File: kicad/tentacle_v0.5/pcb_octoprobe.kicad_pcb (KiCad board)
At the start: 2 copper layers, 100 x 165 mm, 736 parts, among them J101 USB-226-BRW, J1302 Conn_02x20, J1303 Conn_02x20, J1501 Conn_02x20, J1502 Conn_01x12, J201 Conn_02x05, J301 USB_C_Receptacle_USB2.0, J501 Conn_02x20, U1001 GAQY221S, U1101 GAQY221S, U1201 GAQY221S, U1401 MT9700, U1501 RP2040, U1502 W25Q32JVS, U1503 TXB0108PW, U201 RP2040, U202 AMS1117-3.3, U203 W25Q32JVS, U301 AMS1117-3.3, U302 USB2514B_Bi, U401 MT9700, U601 GAQY221S, U701 GAQY221S, U801 GAQY221S, U901 GAQY221S, X201 Oscillator-12MHz, Y301 24MHz

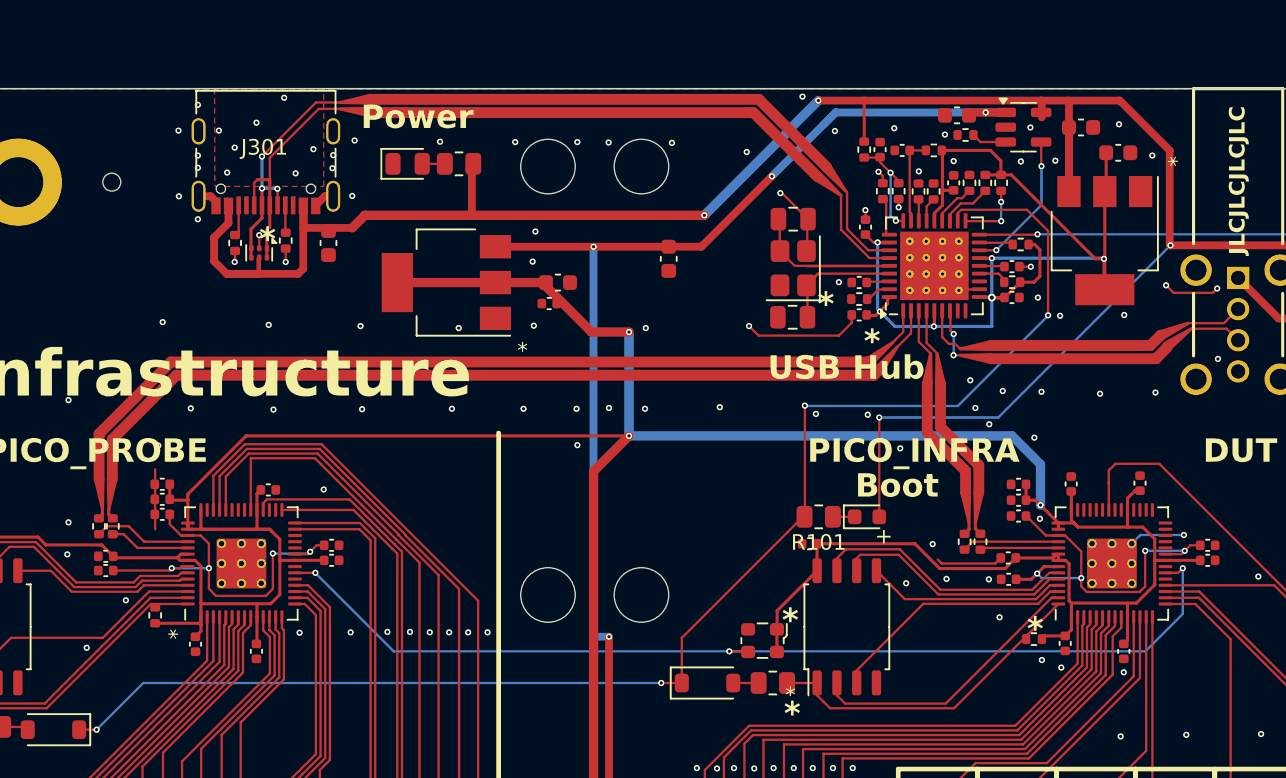
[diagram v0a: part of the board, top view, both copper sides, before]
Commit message: Footprint 'USB Differential': Increase distance
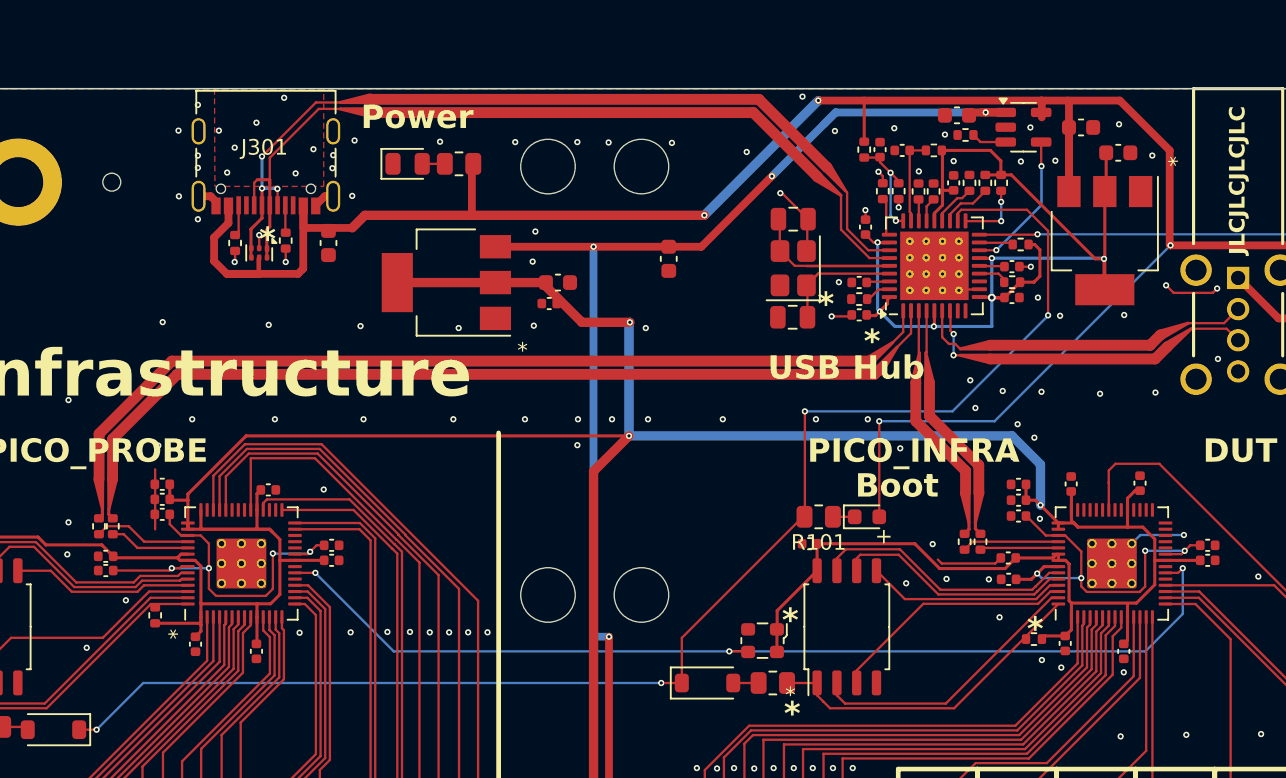
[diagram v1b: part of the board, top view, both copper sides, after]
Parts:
- NT101, NT102, NT103, NT104, NT105, NT106, NT301, NT302: value octoprobe_NetTie_USB_Differential -> NetTie-4_USB_Differential
- moved NT103 0.72 mm to (122.8, 35.2)
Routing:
- net GND: track 192.2 -> 185.9 mm

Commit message: Breadboard: Remove pads from schematic
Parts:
- removed BP1301 (x46): prototype_GND, 00_project_library:octoprobe_breakout_PB
- removed C1401, C1402, C311, C312, C402: 10u, Capacitor_SMD:C_0603_1608Metric
- removed H1301, H1302, H1303, H1304: octoprobe_CableTieHole, 00_project_library:octoprobe_CableTieHole
- removed J101: USB-226-BRW, 00_project_library:USB226BRW
- removed R1401, R401: 10k, Resistor_SMD:R_0402_1005Metric
- removed U1401, U401: MT9700, Package_TO_SOT_SMD:SOT-23-5
- removed U301: AMS1117-3.3, 00_project_library:SOT-223-3_TabPin2
- added ?: prototype_NC, 00_project_library:octoprobe_breakout_PB_NC, F.Cu at (99.4, 106.2)
- added ?: prototype_NC, 00_project_library:octoprobe_breakout_PB_NC, F.Cu at (132.4, 108.7)
- added ?: prototype_NC, 00_project_library:octoprobe_breakout_PB_NC, F.Cu at (132.4, 113.8)
- added ?: prototype_NC, 00_project_library:octoprobe_breakout_PB_NC, F.Cu at (76.5, 106.2)
- added ?: prototype_NC, 00_project_library:octoprobe_breakout_PB_NC, F.Cu at (132.4, 134.1)
- added ?: prototype_NC, 00_project_library:octoprobe_breakout_PB_NC, F.Cu at (86.7, 106.2)
- added ?: prototype_NC, 00_project_library:octoprobe_breakout_PB_NC, F.Cu at (114.6, 106.2)
- added ?: prototype_NC, 00_project_library:octoprobe_breakout_PB_NC, F.Cu at (109.6, 106.2)
- added ?: prototype_NC, 00_project_library:octoprobe_breakout_PB_NC, F.Cu at (84.2, 106.2)
- added ?: prototype_NC, 00_project_library:octoprobe_breakout_PB_NC, F.Cu at (132.4, 126.5)
- added ?: prototype_NC, 00_project_library:octoprobe_breakout_PB_NC, F.Cu at (132.4, 129.0)
- added ?: prototype_NC, 00_project_library:octoprobe_breakout_PB_NC, F.Cu at (117.2, 106.2)
- added ?: prototype_NC, 00_project_library:octoprobe_breakout_PB_NC, F.Cu at (101.9, 106.2)
- added ?: prototype_NC, 00_project_library:octoprobe_breakout_PB_NC, F.Cu at (63.8, 106.2)
- added ?: prototype_NC, 00_project_library:octoprobe_breakout_PB_NC, F.Cu at (132.4, 146.8)
- added ?: prototype_NC, 00_project_library:octoprobe_breakout_PB_NC, F.Cu at (132.4, 131.5)
- added ?: prototype_NC, 00_project_library:octoprobe_breakout_PB_NC, F.Cu at (91.8, 106.2)
- added ?: prototype_NC, 00_project_library:octoprobe_breakout_PB_NC, F.Cu at (132.4, 123.9)
- added ?: prototype_NC, 00_project_library:octoprobe_breakout_PB_NC, F.Cu at (132.4, 106.2)
- added ?: prototype_NC, 00_project_library:octoprobe_breakout_PB_NC, F.Cu at (132.4, 116.3)
- added ?: prototype_NC, 00_project_library:octoprobe_breakout_PB_NC, F.Cu at (127.3, 106.2)
- added ?: prototype_NC, 00_project_library:octoprobe_breakout_PB_NC, F.Cu at (122.3, 106.2)
- added ?: prototype_NC, 00_project_library:octoprobe_breakout_PB_NC, F.Cu at (112.1, 106.2)
- added ?: prototype_NC, 00_project_library:octoprobe_breakout_PB_NC, F.Cu at (132.4, 149.3)
- added ?: prototype_NC, 00_project_library:octoprobe_breakout_PB_NC, F.Cu at (119.7, 106.2)
- added ?: prototype_NC, 00_project_library:octoprobe_breakout_PB_NC, F.Cu at (89.2, 106.2)
- added ?: prototype_NC, 00_project_library:octoprobe_breakout_PB_NC, F.Cu at (79.1, 106.2)
- added ?: prototype_NC, 00_project_library:octoprobe_breakout_PB_NC, F.Cu at (104.5, 106.2)
- added ?: prototype_NC, 00_project_library:octoprobe_breakout_PB_NC, F.Cu at (132.4, 136.6)
- added ?: prototype_NC, 00_project_library:octoprobe_breakout_PB_NC, F.Cu at (94.3, 106.2)
- added ?: prototype_NC, 00_project_library:octoprobe_breakout_PB_NC, F.Cu at (132.4, 151.9)
- added ?: prototype_NC, 00_project_library:octoprobe_breakout_PB_NC, F.Cu at (132.4, 121.4)
- added ?: prototype_NC, 00_project_library:octoprobe_breakout_PB_NC, F.Cu at (96.9, 106.2)
- added ?: prototype_NC, 00_project_library:octoprobe_breakout_PB_NC, F.Cu at (66.4, 106.2)
- added ?: prototype_NC, 00_project_library:octoprobe_breakout_PB_NC, F.Cu at (81.6, 106.2)
- added ?: prototype_NC, 00_project_library:octoprobe_breakout_PB_NC, F.Cu at (107.0, 106.2)
- added ?: prototype_NC, 00_project_library:octoprobe_breakout_PB_NC, F.Cu at (132.4, 111.2)
- added ?: prototype_NC, 00_project_library:octoprobe_breakout_PB_NC, F.Cu at (132.4, 141.7)
- added ?: prototype_NC, 00_project_library:octoprobe_breakout_PB_NC, F.Cu at (68.9, 106.2)
- added ?: prototype_NC, 00_project_library:octoprobe_breakout_PB_NC, F.Cu at (129.9, 106.2)
- added ?: prototype_NC, 00_project_library:octoprobe_breakout_PB_NC, F.Cu at (71.5, 106.2)
- added ?: prototype_NC, 00_project_library:octoprobe_breakout_PB_NC, F.Cu at (132.4, 118.8)
- added ?: prototype_NC, 00_project_library:octoprobe_breakout_PB_NC, F.Cu at (74.0, 106.2)
- added ?: prototype_NC, 00_project_library:octoprobe_breakout_PB_NC, F.Cu at (132.4, 144.2)
- added ?: prototype_NC, 00_project_library:octoprobe_breakout_PB_NC, F.Cu at (124.8, 106.2)
- added ?: prototype_NC, 00_project_library:octoprobe_breakout_PB_NC, F.Cu at (132.4, 139.2)
- added BP201: octoprobe_prototype_board, 00_project_library:octoprobe_breakout_PB, F.Cu at (184.6, 44.2)
- added BP202: octoprobe_prototype_board, 00_project_library:octoprobe_breakout_PB, F.Cu at (184.6, 48.2)
- added C215: 10u, Capacitor_SMD:C_0603_1608Metric, F.Cu at (89.4, 22.0)
- added C216: 470u, Capacitor_SMD:C_Elec_6.3x5.8, F.Cu at (135.8, 21.3)
- added C217: 10u, Capacitor_SMD:C_0603_1608Metric, F.Cu at (170.7, 39.5)
- added C218: 10u, Capacitor_SMD:C_0603_1608Metric, F.Cu at (168.4, 43.7)
- added D103: green, LED_SMD:LED_0805_2012Metric, F.Cu at (202.6, 56.7)
- added D104: green, LED_SMD:LED_0805_2012Metric, F.Cu at (202.6, 59.7)
- added J202: Conn_01x5, 00_project_library:PinSocket_1x5_P2.54mm_Vertical_squarepad_USB, F.Cu at (108.1, 43.7)
- added R206: 10k, Resistor_SMD:R_0402_1005Metric, F.Cu at (148.2, 46.3)
- added R208: 2K7, Resistor_SMD:R_0402_1005Metric, F.Cu at (92.6, 24.1)
- added R209: 3K6, Resistor_SMD:R_0402_1005Metric, F.Cu at (177.3, 35.8)
- added R210: 12k, Resistor_SMD:R_0402_1005Metric, F.Cu at (178.2, 29.1)
- added U204: TPS2595xx, Package_SON:WSON-8-1EP_2x2mm_P0.5mm_EP0.9x1.6mm, F.Cu at (89.4, 24.4)
- added U205: TPS2595xx, Package_SON:WSON-8-1EP_2x2mm_P0.5mm_EP0.9x1.6mm, F.Cu at (170.8, 34.2)
- added U206: MT9700, Package_TO_SOT_SMD:SOT-23-5, F.Cu at (178.2, 23.0)
- NT101, NT102, NT103, NT104, NT105, NT106, NT301, NT302: value NetTie-4_USB_Differential -> octoprobe_NetTie_USB_Differential
- moved R103 131.9 mm to (166.0, 86.0)
- moved C401 127.5 mm to (208.8, 56.4), turned to 0 degrees
- moved C202 98.9 mm to (184.9, -20.1)
- moved R104 90.6 mm to (174.6, 90.2)
- moved C201 74.0 mm to (154.8, -27.9), turned to 0 degrees
- moved Logo_open_hardware101 70.7 mm to (221.1, 30.6)
- moved R1501 64.3 mm to (135.2, 45.4)
- moved R1502 64.3 mm to (134.3, 45.4)
- moved NT102 63.4 mm to (133.8, 43.3), turned to 135 degrees
- moved C1501 63.3 mm to (148.2, 47.2)
- moved C1508 63.3 mm to (148.2, 48.2)
- moved C1502 63.2 mm to (133.5, 48.2)
- moved C1505 63.2 mm to (133.5, 47.3)
- moved D1501 63.2 mm to (130.2, 58.4)
- moved J1501 63.2 mm to (128.3, 66.0)
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- renumbered BP1302 to ?, BP1301 to ?
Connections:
- C1504 pad 1: +3V3 -> +3V3infra
- C1505 pad 1: +3V3 -> +3V3infra
- C1506 pad 1: +3V3 -> +3V3infra
- C1507 pad 1: +3V3 -> +3V3infra
- C1508 pad 1: +3V3 -> +3V3infra
- C1509 pad 1: +3V3 -> +3V3infra
- C1510 pad 2: +3V3 -> +3V3infra
- C1511 pad 1: +3V3 -> +3V3infra
- C1512 pad 1: +3V3 -> +3V3infra
- C201 pad 1: +5V -> +5Vbuf
- C206 pad 1: +3V3 -> +3V3infra
- C207 pad 1: +3V3 -> +3V3infra
- C208 pad 1: +3V3 -> +3V3infra
- C209 pad 1: +3V3 -> +3V3infra
- C210 pad 1: +3V3 -> +3V3infra
- C211 pad 1: +3V3 -> +3V3infra
- C212 pad 2: +3V3 -> +3V3infra
- C213 pad 1: +3V3 -> +3V3infra
- C214 pad 1: +3V3 -> +3V3infra
- C301 pad 1: HUB+3V3 -> +3V3
- C302 pad 1: HUB+3V3 -> +3V3
- C303 pad 1: HUB+3V3 -> +3V3
- C304 pad 1: HUB+3V3 -> +3V3
- D1501 pad 1: RP2_BOOT -> RP2_PROBE_BOOT
- D202 pad 1: RP2_BOOT -> RP2_INFRA_BOOT
- J1502 pad 12: +3V3 -> +3V3infra
- J201 pad 10: +5V -> +5Vbuf
- J201 pad 9: +5V -> +5Vbuf
- J501 pad 12: +3V3 -> +3V3infra
- J501 pad 16: +3V3 -> +3V3infra
- J501 pad 20: +3V3 -> +3V3infra
- J501 pad 24: +3V3 -> +3V3infra
- J501 pad 28: +3V3 -> +3V3infra
- J501 pad 4: +3V3 -> +3V3infra
- J501 pad 8: +3V3 -> +3V3infra
- NT101 pad 1: /USB Hub Chip/USB_DP1 -> /USB Hub Chip/USB_DP4
- NT101 pad 3: /USB Hub Chip/USB_DM1 -> /USB Hub Chip/USB_DM4
- NT103 pad 1: /USB Hub Chip/USB_DP2 -> /USB Hub Chip/USB_DP1
- NT103 pad 3: /USB Hub Chip/USB_DM2 -> /USB Hub Chip/USB_DM1
- NT105 pad 1: /USB Hub Chip/USB_DM3 -> /USB Hub Chip/USB_DP3
- NT105 pad 3: /USB Hub Chip/USB_DP3 -> /USB Hub Chip/USB_DM3
- R101 pad 2: RP2_BOOT -> RP2_INFRA_BOOT
- R103 pad 2: /USB Power Switch DUT/VOUT -> +3V3dut
- R104 pad 2: +5V -> +3V3infra
- R1504 pad 1: +3V3 -> +3V3infra
- R204 pad 2: Net-(U201-GPIO15) -> Net-(U201-GPIO20)
- R207 pad 1: +3V3 -> +3V3infra
- R304 pad 2: HUB+3V3 -> +3V3
- R312 pad 1: HUB+3V3 -> +3V3
- R313 pad 1: HUB+3V3 -> +3V3
- R314 pad 1: HUB+3V3 -> +3V3
- R315 pad 1: HUB+3V3 -> +3V3
- U1501 pad 1: +3V3 -> +3V3infra
- U1501 pad 10: +3V3 -> +3V3infra
- U1501 pad 22: +3V3 -> +3V3infra
- U1501 pad 26: unconnected-(U1501-RUN-Pad26) -> RP2_PROBE_RUN
- U1501 pad 33: +3V3 -> +3V3infra
- U1501 pad 42: +3V3 -> +3V3infra
- U1501 pad 43: +3V3 -> +3V3infra
- U1501 pad 44: +3V3 -> +3V3infra
- U1501 pad 48: +3V3 -> +3V3infra
- U1501 pad 49: +3V3 -> +3V3infra
- U1502 pad 8: +3V3 -> +3V3infra
- U1503 pad 2: +3V3 -> +3V3infra
- U201 pad 1: +3V3 -> +3V3infra
- U201 pad 10: +3V3 -> +3V3infra
- U201 pad 11: RELAIS_1 -> unconnected-(U201-GPIO8-Pad11)
- U201 pad 12: RELAIS_2 -> unconnected-(U201-GPIO9-Pad12)
- U201 pad 13: RELAIS_3 -> Net-(J201-Pin_1)
- U201 pad 14: RELAIS_4 -> Net-(J201-Pin_3)
- U201 pad 15: RELAIS_5 -> Net-(J201-Pin_5)
- U201 pad 16: RELAIS_6 -> Net-(J201-Pin_7)
- U201 pad 17: RELAIS_7 -> Net-(J201-Pin_2)
- U201 pad 18: Net-(U201-GPIO15) -> Net-(J201-Pin_4)
- U201 pad 2: Net-(J201-Pin_1) -> unconnected-(U201-GPIO0-Pad2)
- U201 pad 22: +3V3 -> +3V3infra
- U201 pad 27: unconnected-(U201-GPIO16-Pad27) -> Net-(J201-Pin_6)
- U201 pad 28: unconnected-(U201-GPIO17-Pad28) -> Net-(J201-Pin_8)
- U201 pad 3: Net-(J201-Pin_2) -> RELAIS_1
- U201 pad 31: unconnected-(U201-GPIO20-Pad31) -> Net-(U201-GPIO20)
- U201 pad 32: unconnected-(U201-GPIO21-Pad32) -> RP2_PROBE_BOOT
- U201 pad 33: +3V3 -> +3V3infra
- U201 pad 34: unconnected-(U201-GPIO22-Pad34) -> RP2_PROBE_RUN
- U201 pad 35: unconnected-(U201-GPIO23-Pad35) -> DUT_PWR_EN
- U201 pad 4: Net-(J201-Pin_3) -> RELAIS_2
- U201 pad 42: +3V3 -> +3V3infra
- U201 pad 43: +3V3 -> +3V3infra
- U201 pad 44: +3V3 -> +3V3infra
- U201 pad 48: +3V3 -> +3V3infra
- U201 pad 49: +3V3 -> +3V3infra
- U201 pad 5: Net-(J201-Pin_4) -> RELAIS_3
- U201 pad 6: Net-(J201-Pin_5) -> RELAIS_4
- U201 pad 7: Net-(J201-Pin_6) -> RELAIS_5
- U201 pad 8: Net-(J201-Pin_7) -> RELAIS_6
- U201 pad 9: Net-(J201-Pin_8) -> RELAIS_7
- U202 pad 3: +5V -> +5Vbuf
- U203 pad 8: +3V3 -> +3V3infra
- U302 pad 10: HUB+3V3 -> +3V3
- U302 pad 12: /USB1_PWR -> RP2_INFRA_PWR_EN
- U302 pad 15: HUB+3V3 -> +3V3
- U302 pad 16: /USB2_PWR -> RP2_INFRA_BOOT
- U302 pad 18: /USB3_PWR -> /USB Hub Chip/PRT_PWR3
- U302 pad 20: RP2_BOOT -> /USB Hub Chip/PRT_PWR4
- U302 pad 23: HUB+3V3 -> +3V3
- U302 pad 29: HUB+3V3 -> +3V3
- U302 pad 36: HUB+3V3 -> +3V3
- U302 pad 5: HUB+3V3 -> +3V3
- X201 pad 1: +3V3 -> +3V3infra
- X201 pad 4: +3V3 -> +3V3infra
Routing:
- net +3V3: track 386.3 -> 41.5 mm, vias 3 -> 5
- net +3V3infra: track 0.00 -> 257.9 mm, vias 0 -> 2
- net +5V: track 253.1 -> 0.00 mm, vias 6 -> 0
- net /USB Power Switch DUT/VOUT: track 249.0 -> 0.00 mm
- net Net-(U201-GPIO15): track 204.3 -> 0.00 mm
- net Net-(U201-GPIO20): track 0.00 -> 103.6 mm
- net RP2_BOOT: track 91.2 -> 0.00 mm, vias 4 -> 0
- net (no net): track 0.00 -> 87.9 mm, vias 0 -> 1
- net HUB+3V3: track 66.9 -> 0.00 mm, vias 6 -> 0
- net HUB+5V: track 144.3 -> 79.1 mm, vias 4 -> 2
- net Net-(U201-GPIO24): track 208.6 -> 148.2 mm
- net /USB_PROBE_D-: track 54.3 -> 14.7 mm
- net /USB_PROBE_D+: track 53.6 -> 14.7 mm
- net DUT_PWR_EN: track 0.00 -> 38.2 mm, vias 0 -> 1
- net /USB_INFRA_D-: track 8.38 -> 38.6 mm
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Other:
- board text added: "DUT USB"
